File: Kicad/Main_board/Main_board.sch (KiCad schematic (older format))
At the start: 27 parts, among them J1 LIPO 2S, J10 DIST_FRONT, J11 SENSORES_LINEA, J12 DIST_DCHA, J2 MOT_IZQ, J3 TB6612FNG_A, J4 TB6612FNG_B, J5 DC-DC_5V, J6 HC-05, J7 MOT_DER, J8 DIST_IZQ, J9 CAMARA, SW1 SW_DPDT, SW2 SW_Push, SW3 SW_Push, U1 PCF8574

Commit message: BOMs and PDF schematic added
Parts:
- D3: value 1N4003 -> 1N4001
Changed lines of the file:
@@
 P 6450 4500
 F 0 "D3" H 6450 4600 50  0000 C CNN
-F 1 "1N4003" H 6450 4400 50  0000 C CNN
+F 1 "1N4001" H 6450 4400 50  0000 C CNN
 F 2 "Diodes_THT:D_A-405_P10.16mm_Horizontal" H 6450 4500 50  0001 C CNN
 F 3 "" H 6450 4500 50  0001 C CNN

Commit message: Resistors modified
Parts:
- R1, R2: value 1k -> 220
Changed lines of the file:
@@
 P 1500 4250
 F 0 "R1" V 1580 4250 50  0000 C CNN
-F 1 "1k" V 1500 4250 50  0000 C CNN
+F 1 "220" V 1500 4250 50  0000 C CNN
 F 2 "Resistors_THT:R_Axial_DIN0207_L6.3mm_D2.5mm_P10.16mm_Horizontal" V 1430 4250 50  0001 C CNN
 F 3 "" H 1500 4250 50  0001 C CNN
@@
 P 1900 4250
 F 0 "R2" V 1980 4250 50  0000 C CNN
-F 1 "1k" V 1900 4250 50  0000 C CNN
+F 1 "220" V 1900 4250 50  0000 C CNN
 F 2 "Resistors_THT:R_Axial_DIN0207_L6.3mm_D2.5mm_P10.16mm_Horizontal" V 1830 4250 50  0001 C CNN
 F 3 "" H 1900 4250 50  0001 C CNN

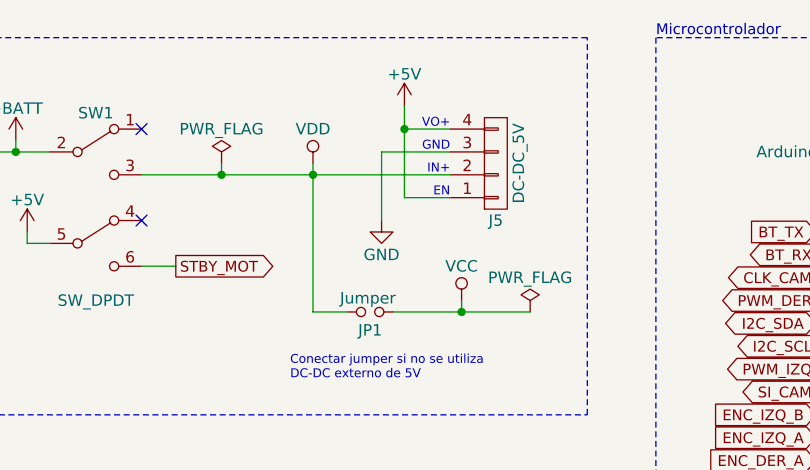
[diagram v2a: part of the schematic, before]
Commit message: DC-DC enable modified
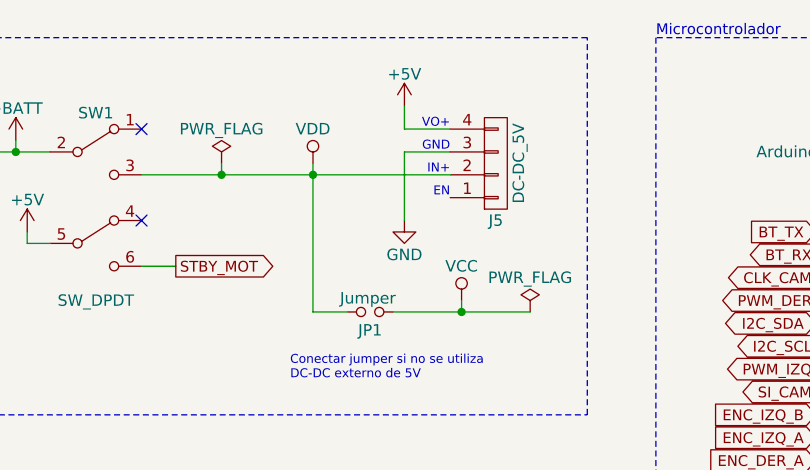
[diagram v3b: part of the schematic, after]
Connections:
- net +5V: no longer J5.1 (P1)
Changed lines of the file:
@@
 L GND #PWR022
 U 1 1 593E6398
-P 3600 1600
-F 0 "#PWR022" H 3600 1350 50  0001 C CNN
-F 1 "GND" H 3600 1450 50  0000 C CNN
-F 2 "" H 3600 1600 50  0001 C CNN
-F 3 "" H 3600 1600 50  0001 C CNN
-	1    3600 1600
+P 3700 1600
+F 0 "#PWR022" H 3700 1350 50  0001 C CNN
+F 1 "GND" H 3700 1450 50  0000 C CNN
+F 2 "" H 3700 1600 50  0001 C CNN
+F 3 "" H 3700 1600 50  0001 C CNN
+	1    3700 1600
 	1    0    0    -1
 $EndComp
@@
 GND
 Wire Wire Line
-	3600 1600 3600 1300
-Wire Wire Line
-	3600 1300 3900 1300
+	3700 1600 3700 1300
+Wire Wire Line
+	3700 1300 3900 1300
 Wire Wire Line
 	3900 1200 3700 1200
-Wire Wire Line
-	3700 1100 3700 1500
 Connection ~ 3300 1400
 $Comp
@@
 Text Notes 3200 2300 0    39   ~ 0
 Conectar jumper si no se utiliza\nDC-DC externo de 5V
-Wire Wire Line
-	3700 1500 3900 1500
-Connection ~ 3700 1200
 Wire Wire Line
 	5500 1650 5600 1650
@@
 	1    0    0    -1
 $EndComp
+Wire Wire Line
+	3700 1200 3700 1100
 $EndSCHEMATC
